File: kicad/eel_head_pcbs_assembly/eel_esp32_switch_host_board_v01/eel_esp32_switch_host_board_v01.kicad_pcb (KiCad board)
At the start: 2 copper layers, 53.1 x 24.4 mm, 23 parts, among them J1 Conn_01x02_Female, J2 motor_l, J3 motor_r, J4 neopixels, J5 n00ds, U1 XIAO-ESP32C3, U2 DRV8833, U3 ep2_txco_rx, U4 5v_0.6a_boost_converter, U5 FMBM5551, U6 FMBM5551

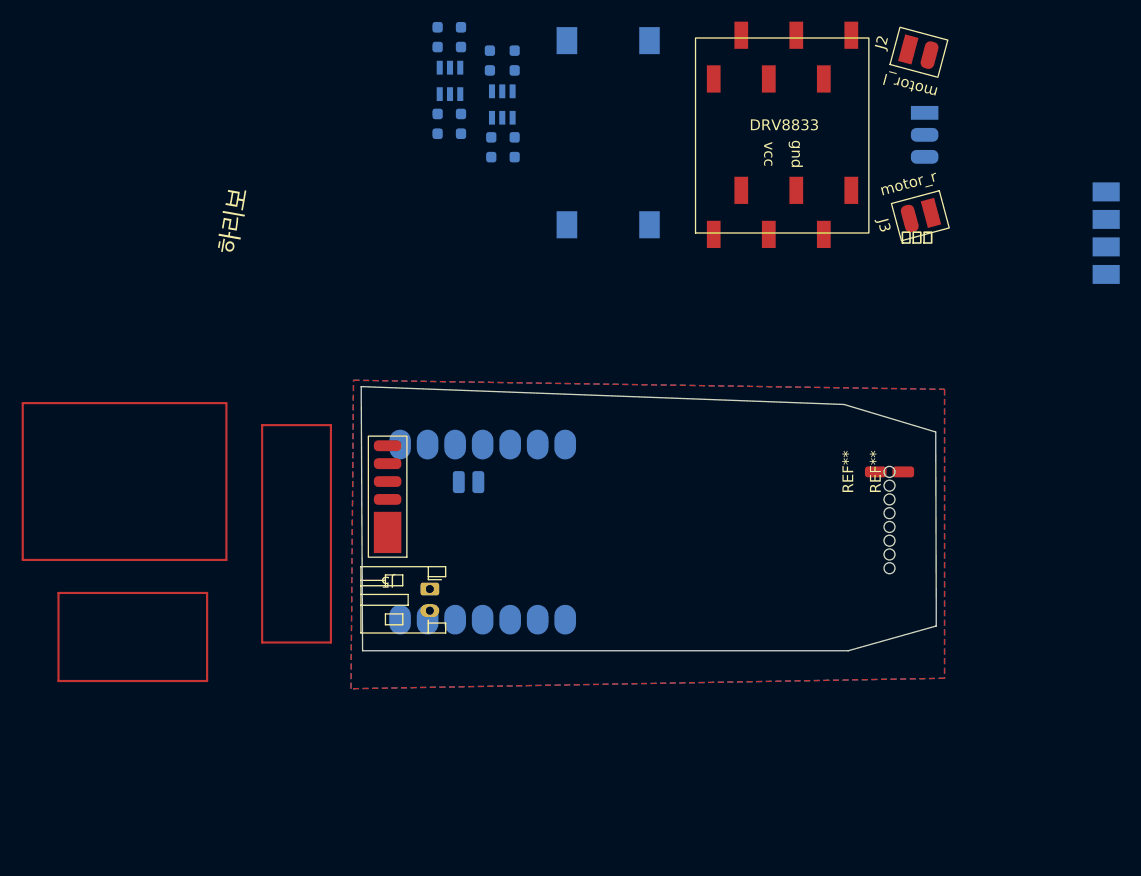
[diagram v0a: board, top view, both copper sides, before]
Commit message: create pcb just for esp32 and on/off switch
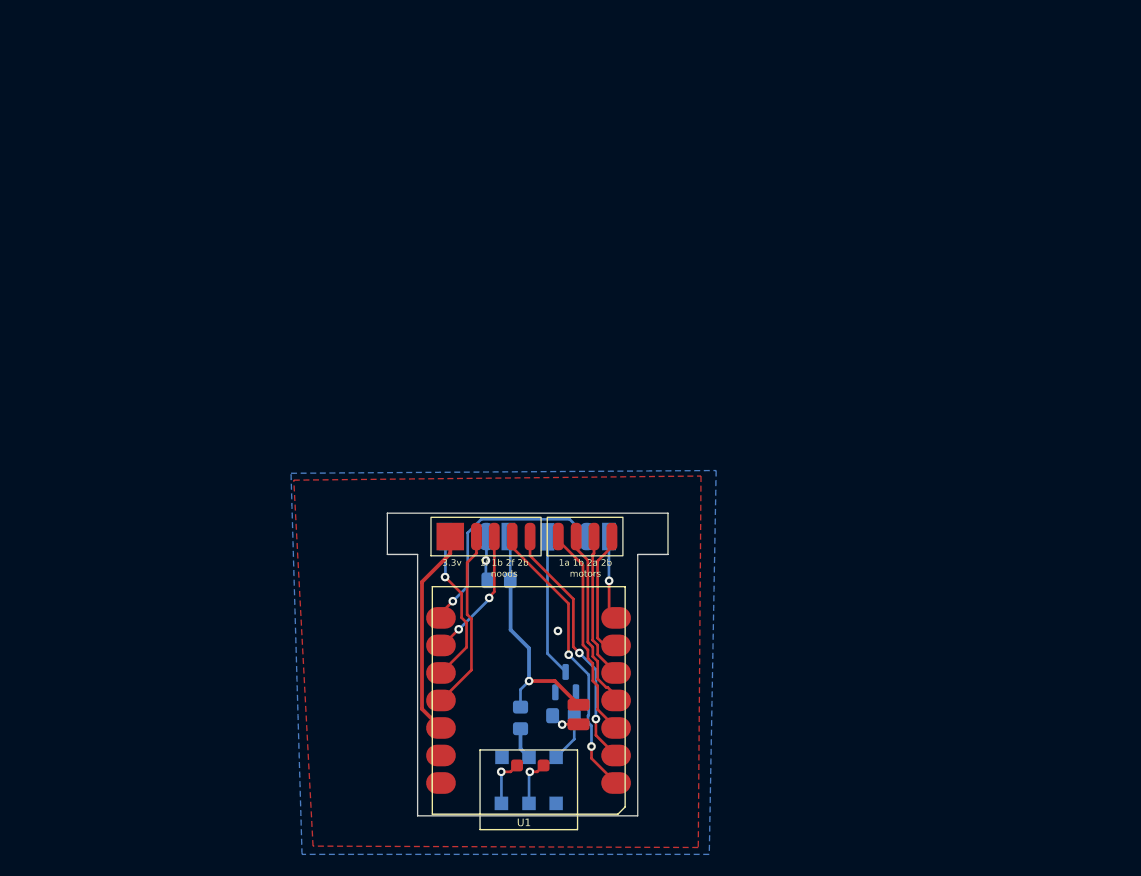
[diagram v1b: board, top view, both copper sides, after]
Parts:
- removed R3, R4, R7, R8: 100, Resistor_SMD:R_0603_1608Metric_Pad0.98x0.95mm_HandSolder
- removed R5, R6: 220, Resistor_SMD:R_0603_1608Metric_Pad0.98x0.95mm_HandSolder
- removed REF** (x2): SolderWirePad_1x01_SMD_1x2mm, Connector_Wire:SolderWirePad_1x01_SMD_1x2mm
- removed U2: DRV8833, haribo_kimchi_boards:drv8833_breakout
- removed U3: ep2_txco_rx, haribo_kimchi_boards:happymodel_ep2_txco_rx
- removed U4: 5v_0.6a_boost_converter, haribo_kimchi_boards:5v_0.6a_boost_converter
- removed U5, U6: FMBM5551, haribo_kimchi_extra_footprints:SSOT6_3X1P7_ONS
- removed haribo_korean: LOGO, haribo_kimchi_pcbgfx:haribo_in_korean_3.2mm
- removed logo_haribo_bear: LOGO, haribo_kimchi_pcbgfx:haribo_outline_bw_8mm
- added C1: C, Capacitor_SMD:C_0805_2012Metric_Pad1.18x1.45mm_HandSolder, B.Cu at (92.2, 87.5)
- added G***: LOGO, haribo_kimchi_pcbgfx:haribo_outline_bw_8mm, B.Cu at (89.0, 98.2)
- added J6: n00ds, haribo_kimchi_boards:smd_solder_pads_1x05_n00ds_v3_smaller, F.Cu at (84.2, 83.4)
- added Q1: BC817, Package_TO_SOT_SMD:SOT-23, B.Cu at (98.4, 96.9)
- added SW1: SW_Push_DPDT, haribo_kimchi_extra_footprints:Nidec_2x03_dpdt_CL-SB-22B-11, B.Cu at (95.0, 105.9)
- J1: footprint Connector_JST:JST_PH_S2B-PH-K_1x02_P2.00mm_Horizontal -> haribo_kimchi_boards:smd_solder_pads_1x02_2.54mm; moved to B.Cu
- J2: value motor_l -> motor driver; footprint haribo_kimchi_boards:smd_solder_pads_1x02_2.54mm -> haribo_kimchi_boards:smd_solder_pads_1x04
- J3: value motor_r -> ELRS RX; moved to B.Cu
- J4: value neopixels -> V_RET; footprint haribo_kimchi_boards:smd_solder_pads_1x03_2.54mm -> haribo_kimchi_boards:smd_solder_pads_1x01_2.54mm
- J5: value n00ds -> RGB_DATA; footprint haribo_kimchi_boards:smd_solder_pads_1x05_n00ds_v2_smaller -> haribo_kimchi_boards:smd_solder_pads_1x01_2.54mm; moved to B.Cu
- R1, R2: value 220 -> 330; footprint Resistor_SMD:R_0603_1608Metric_Pad0.98x0.95mm_HandSolder -> Resistor_SMD:R_0805_2012Metric_Pad1.20x1.40mm_HandSolder
- U1: moved to F.Cu
- moved R2 63.7 mm to (98.2, 100.0), turned to 0 degrees
- moved R1 63.1 mm to (94.2, 100.2)
- moved J2 56.3 mm to (94.9, 83.4), turned to 90 degrees
- moved J4 51.4 mm to (94.7, 83.5), turned to -90 degrees
- moved J3 42.5 mm to (104.4, 83.4), turned to 90 degrees
- moved U1 14.2 mm to (103.9, 88.1), turned to 180 degrees
- moved J1 10.5 mm to (95.1, 83.4), turned to 90 degrees
- moved J5 4.95 mm to (85.2, 83.4), turned to -90 degrees
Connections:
- J2 pad 1: motor2_out1 -> motor2_2
- J2 pad 2: motor2_out2 -> motor2_1
- J3 pad 1: motor1_out1 -> XIAO_TX
- J3 pad 2: motor1_out2 -> XIAO_RX
- J4 pad 1: +5V -> V_RET
- J5 pad 1: +3V3 -> NEOPIXEL_DATA
- R1 pad 1: nood1_2_sig -> +BATT
- R2 pad 1: nood1_1_sig -> GND
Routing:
- net nood1_2_sig: track 0.00 -> 26.8 mm, vias 0 -> 2
- net nood1_1_sig: track 0.00 -> 23.5 mm, vias 0 -> 2
- net +BATT: track 0.00 -> 22.3 mm, vias 0 -> 1
- net XIAO_RX: track 0.00 -> 21.1 mm, vias 0 -> 1
- net motor2_2: track 0.00 -> 19.9 mm
- net +3V3: track 0.00 -> 19.5 mm
- net nood2_2_sig: track 0.00 -> 16.8 mm
- net motor2_1: track 0.00 -> 16.7 mm
- net NEOPIXEL_DATA: track 0.00 -> 14.4 mm, vias 0 -> 1
- net motor1_2: track 0.00 -> 13.5 mm
- net V_RET: track 0.00 -> 13.2 mm
- net nood2_1_sig: track 0.00 -> 12.2 mm, vias 0 -> 2
- net motor1_1: track 0.00 -> 11.9 mm
- net GND: track 0.00 -> 11.6 mm, vias 0 -> 4
- net XIAO_TX: track 0.00 -> 7.78 mm, vias 0 -> 1
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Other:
- board size 53.1 x 24.4 mm -> 25.9 x 27.9 mm
- board text added: "1a 1b 2a 2b"
- board text added: "1f 1b 2f 2b"
- board text added: "3.3v"
- board text added: "Eel connector pcb v0.5 2024-02-23 (c) Adriaan Wormgoor"
- board text added: "Vret"
- board text added: "motors"
- board text added: "noods"
- board text added: "rcvr"
- board text added: "rx tx"
- board text added: "vbat gnd"
- board text added: "~rgb"
- board text removed: "하리보"

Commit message: final touches initial pcb design
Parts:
- R2: value 330 -> 1k
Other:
- outline, holes or cut-outs redrawn
